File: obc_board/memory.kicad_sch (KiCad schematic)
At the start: 10 parts

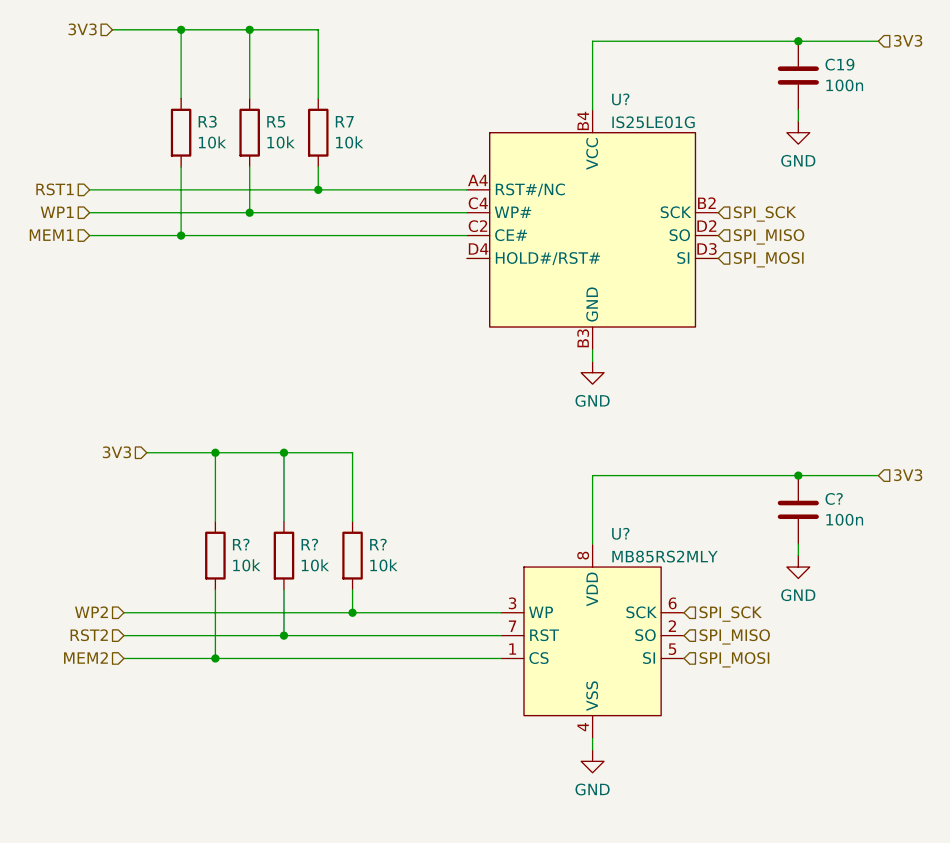
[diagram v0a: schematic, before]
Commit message: changed magnetorquer driver IC and changed power switch IC
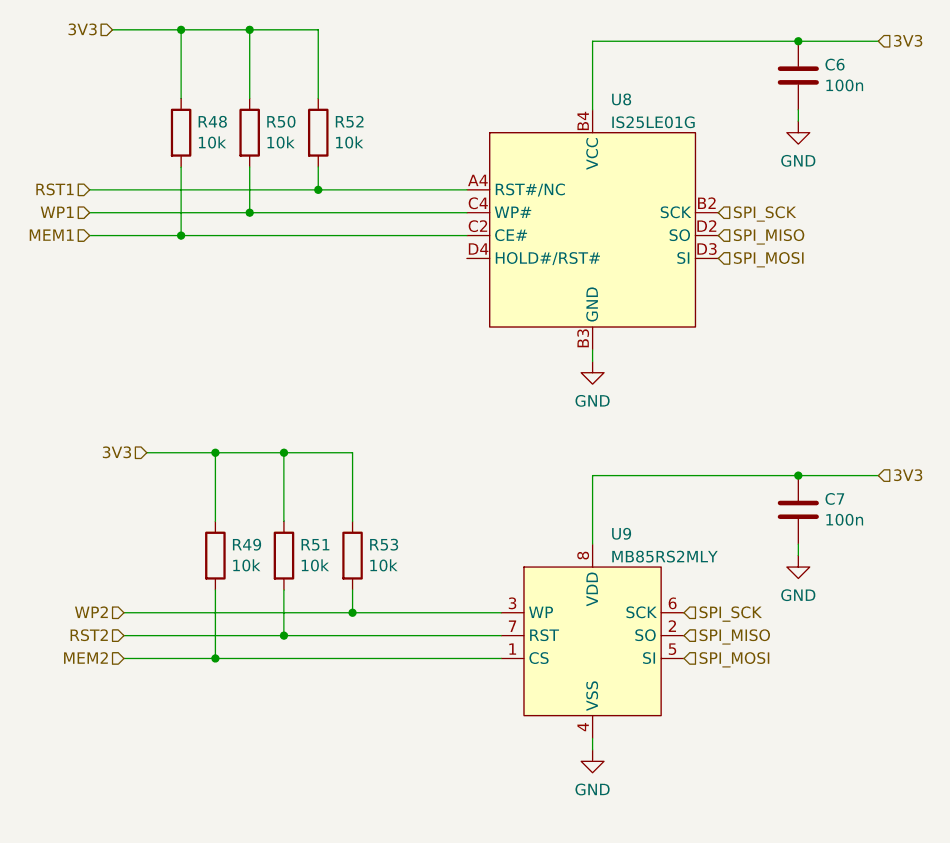
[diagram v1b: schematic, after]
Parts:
- gave numbers to parts that had none: 6
- renumbered C19 to C6, R3 to R48, R5 to R50, R7 to R52
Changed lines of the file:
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@@
   (symbol (lib_id "Device:C") (at 154.94 55.88 0) (unit 1)
     (in_bom yes) (on_board yes)
-    (property "Reference" "C19" (id 0) (at 157.861 54.7116 0)
+    (property "Reference" "C6" (id 0) (at 157.861 54.7116 0)
       (effects (font (size 1.27 1.27)) (justify left))
     )
@@
   (symbol (lib_id "Device:R") (at 101.6 62.23 0) (unit 1)
     (in_bom yes) (on_board yes)
-    (property "Reference" "R7" (id 0) (at 103.378 61.0616 0)
+    (property "Reference" "R52" (id 0) (at 103.378 61.0616 0)
       (effects (font (size 1.27 1.27)) (justify left))
     )
@@
   (symbol (lib_id "Device:R") (at 93.98 62.23 0) (unit 1)
     (in_bom yes) (on_board yes)
-    (property "Reference" "R5" (id 0) (at 95.758 61.0616 0)
+    (property "Reference" "R50" (id 0) (at 95.758 61.0616 0)
       (effects (font (size 1.27 1.27)) (justify left))
     )
@@
   (symbol (lib_id "Device:R") (at 86.36 62.23 0) (unit 1)
     (in_bom yes) (on_board yes)
-    (property "Reference" "R3" (id 0) (at 88.138 61.0616 0)
+    (property "Reference" "R48" (id 0) (at 88.138 61.0616 0)
       (effects (font (size 1.27 1.27)) (justify left))
     )
@@
   (symbol (lib_id "Device:C") (at 154.94 104.14 0) (unit 1)
     (in_bom yes) (on_board yes)
-    (property "Reference" "C?" (id 0) (at 157.861 102.9716 0)
+    (property "Reference" "C7" (id 0) (at 157.861 102.9716 0)
       (effects (font (size 1.27 1.27)) (justify left))
     )
@@
   (symbol (lib_id "power:GND") (at 154.94 109.22 0) (unit 1)
     (in_bom yes) (on_board yes) (fields_autoplaced)
-    (property "Reference" "#PWR?" (id 0) (at 154.94 115.57 0)
+    (property "Reference" "#PWR023" (id 0) (at 154.94 115.57 0)
       (effects (font (size 1.27 1.27)) hide)
     )
@@
   (symbol (lib_id "Device:R") (at 90.17 109.22 0) (unit 1)
     (in_bom yes) (on_board yes)
-    (property "Reference" "R?" (id 0) (at 91.948 108.0516 0)
+    (property "Reference" "R49" (id 0) (at 91.948 108.0516 0)
       (effects (font (size 1.27 1.27)) (justify left))
     )
@@
   (symbol (lib_name "MB85RS2MLY_1") (lib_id "cubesat_obc_lib:MB85RS2MLY") (at 132.08 119.38 0) (unit 1)
     (in_bom yes) (on_board yes) (fields_autoplaced)
-    (property "Reference" "U?" (id 0) (at 134.0994 106.841 0)
+    (property "Reference" "U9" (id 0) (at 134.0994 106.841 0)
       (effects (font (size 1.27 1.27)) (justify left))
     )
@@
   (symbol (lib_id "cubesat_obc_lib:IS25LE01G") (at 132.08 73.66 0) (unit 1)
     (in_bom yes) (on_board yes) (fields_autoplaced)
-    (property "Reference" "U?" (id 0) (at 134.0994 58.581 0)
+    (property "Reference" "U8" (id 0) (at 134.0994 58.581 0)
       (effects (font (size 1.27 1.27)) (justify left))
     )
@@
   (symbol (lib_id "power:GND") (at 132.08 130.81 0) (unit 1)
     (in_bom yes) (on_board yes) (fields_autoplaced)
-    (property "Reference" "#PWR?" (id 0) (at 132.08 137.16 0)
+    (property "Reference" "#PWR021" (id 0) (at 132.08 137.16 0)
       (effects (font (size 1.27 1.27)) hide)
     )
@@
   (symbol (lib_id "power:GND") (at 132.08 87.63 0) (unit 1)
     (in_bom yes) (on_board yes) (fields_autoplaced)
-    (property "Reference" "#PWR?" (id 0) (at 132.08 93.98 0)
+    (property "Reference" "#PWR020" (id 0) (at 132.08 93.98 0)
       (effects (font (size 1.27 1.27)) hide)
     )
@@
   (symbol (lib_id "Device:R") (at 105.41 109.22 0) (unit 1)
     (in_bom yes) (on_board yes)
-    (property "Reference" "R?" (id 0) (at 107.188 108.0516 0)
+    (property "Reference" "R53" (id 0) (at 107.188 108.0516 0)
       (effects (font (size 1.27 1.27)) (justify left))
     )
@@
   (symbol (lib_id "power:GND") (at 154.94 60.96 0) (unit 1)
     (in_bom yes) (on_board yes) (fields_autoplaced)
-    (property "Reference" "#PWR?" (id 0) (at 154.94 67.31 0)
+    (property "Reference" "#PWR022" (id 0) (at 154.94 67.31 0)
       (effects (font (size 1.27 1.27)) hide)
     )
@@
   (symbol (lib_id "Device:R") (at 97.79 109.22 0) (unit 1)
     (in_bom yes) (on_board yes)
-    (property "Reference" "R?" (id 0) (at 99.568 108.0516 0)
-      (effects (font (size 1.27 1.27)) (justify left))
-    )
+    (property "Reference" "R51" (id 0) (at 99.568 108.0516 0)
+      (effects (font (size 1.27 1.27)) (justify left))
+    )

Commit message: updated digikey part numbers and footprints
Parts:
- C6, C7: Digikey Part Number 490-16433-1-ND -> 399-6828-1-ND
- R48, R49, R50, R51, R52, R53: Digikey Part Number 311-10.0KLRCT-ND -> YAG3436CT-ND
- U8: footprint (none) -> cubesat_obc:TFBGA24_5X5_6X8; Digikey Part Number (none) -> 706-IS25LE01G-RILE-ND
- U9: footprint (none) -> Package_SO:SOIC-8_3.9x4.9mm_P1.27mm; Digikey Part Number (none) -> 865-MB85RS2MLYPNF-GS-AWE2-ND
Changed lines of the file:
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@@
       (effects (font (size 1.27 1.27)) hide)
     )
-    (property "Digikey Part Number" "490-16433-1-ND" (id 4) (at 154.94 55.88 0)
+    (property "Digikey Part Number" "399-6828-1-ND" (id 4) (at 154.94 55.88 0)
       (effects (font (size 1.27 1.27)) hide)
     )
@@
       (effects (font (size 1.27 1.27)) hide)
     )
-    (property "Digikey Part Number" "311-10.0KLRCT-ND" (id 4) (at 101.6 62.23 0)
+    (property "Digikey Part Number" "YAG3436CT-ND" (id 4) (at 101.6 62.23 0)
       (effects (font (size 1.27 1.27)) hide)
     )
@@
       (effects (font (size 1.27 1.27)) hide)
     )
-    (property "Digikey Part Number" "311-10.0KLRCT-ND" (id 4) (at 93.98 62.23 0)
+    (property "Digikey Part Number" "YAG3436CT-ND" (id 4) (at 93.98 62.23 0)
       (effects (font (size 1.27 1.27)) hide)
     )
@@
       (effects (font (size 1.27 1.27)) hide)
     )
-    (property "Digikey Part Number" "311-10.0KLRCT-ND" (id 4) (at 86.36 62.23 0)
+    (property "Digikey Part Number" "YAG3436CT-ND" (id 4) (at 86.36 62.23 0)
       (effects (font (size 1.27 1.27)) hide)
     )
@@
       (effects (font (size 1.27 1.27)) hide)
     )
-    (property "Digikey Part Number" "490-16433-1-ND" (id 4) (at 154.94 104.14 0)
+    (property "Digikey Part Number" "399-6828-1-ND" (id 4) (at 154.94 104.14 0)
       (effects (font (size 1.27 1.27)) hide)
     )
@@
       (effects (font (size 1.27 1.27)) hide)
     )
-    (property "Digikey Part Number" "311-10.0KLRCT-ND" (id 4) (at 90.17 109.22 0)
+    (property "Digikey Part Number" "YAG3436CT-ND" (id 4) (at 90.17 109.22 0)
       (effects (font (size 1.27 1.27)) hide)
     )
@@
       (effects (font (size 1.27 1.27)) (justify left))
     )
-    (property "Footprint" "" (id 2) (at 132.08 119.38 0)
-      (effects (font (size 1.27 1.27)) hide)
-    )
-    (property "Datasheet" "" (id 3) (at 132.08 119.38 0)
+    (property "Footprint" "Package_SO:SOIC-8_3.9x4.9mm_P1.27mm" (id 2) (at 132.08 119.38 0)
+      (effects (font (size 1.27 1.27)) hide)
+    )
+    (property "Datasheet" "https://www.fujitsu.com/uk/imagesgig5/MB85RS2MLY-DS501-00062-GS%20-0v1-E_13.pdf" (id 3) (at 132.08 119.38 0)
+      (effects (font (size 1.27 1.27)) hide)
+    )
+    (property "Digikey Part Number" "865-MB85RS2MLYPNF-GS-AWE2-ND" (id 4) (at 132.08 119.38 0)
       (effects (font (size 1.27 1.27)) hide)
     )
@@
       (effects (font (size 1.27 1.27)) (justify left))
     )
-    (property "Footprint" "" (id 2) (at 132.08 73.66 0)
-      (effects (font (size 1.27 1.27)) hide)
-    )
-    (property "Datasheet" "" (id 3) (at 132.08 73.66 0)
+    (property "Footprint" "cubesat_obc:TFBGA24_5X5_6X8" (id 2) (at 132.08 73.66 0)
+      (effects (font (size 1.27 1.27)) hide)
+    )
+    (property "Datasheet" "https://www.issi.com/WW/pdf/25LE-WE01G.pdf" (id 3) (at 132.08 73.66 0)
+      (effects (font (size 1.27 1.27)) hide)
+    )
+    (property "Digikey Part Number" "706-IS25LE01G-RILE-ND" (id 4) (at 132.08 73.66 0)
       (effects (font (size 1.27 1.27)) hide)
     )
@@
       (effects (font (size 1.27 1.27)) hide)
     )
-    (property "Digikey Part Number" "311-10.0KLRCT-ND" (id 4) (at 105.41 109.22 0)
+    (property "Digikey Part Number" "YAG3436CT-ND" (id 4) (at 105.41 109.22 0)
       (effects (font (size 1.27 1.27)) hide)
     )
@@
       (effects (font (size 1.27 1.27)) hide)
     )
-    (property "Digikey Part Number" "311-10.0KLRCT-ND" (id 4) (at 97.79 109.22 0)
-      (effects (font (size 1.27 1.27)) hide)
-    )
+    (property "Digikey Part Number" "YAG3436CT-ND" (id 4) (at 97.79 109.22 0)
+      (effects (font (size 1.27 1.27)) hide)
+    )

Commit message: routed most of board
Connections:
- net at U8.A2 (NC), U8.A3 (NC), U8.A5 (NC)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: no longer U8.E6 (NC)
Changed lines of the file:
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@@
     (pin "2")
   )
-  (symbol (lib_name "MB85RS2MLY_1") (lib_id "cubesat_obc_lib:MB85RS2MLY") (at 132.08 119.38 0) (unit 1)
+  (symbol (lib_id "cubesat_obc_lib:MB85RS2MLY") (at 132.08 119.38 0) (unit 1)
     (in_bom yes) (on_board yes) (fields_autoplaced)
     (property "Reference" "U9" (id 0) (at 134.0994 106.841 0)
@@
     (pin "E4")
     (pin "E5")
-    (pin "E6")
   )
   (symbol (lib_id "power:GND") (at 132.08 130.81 0) (unit 1)

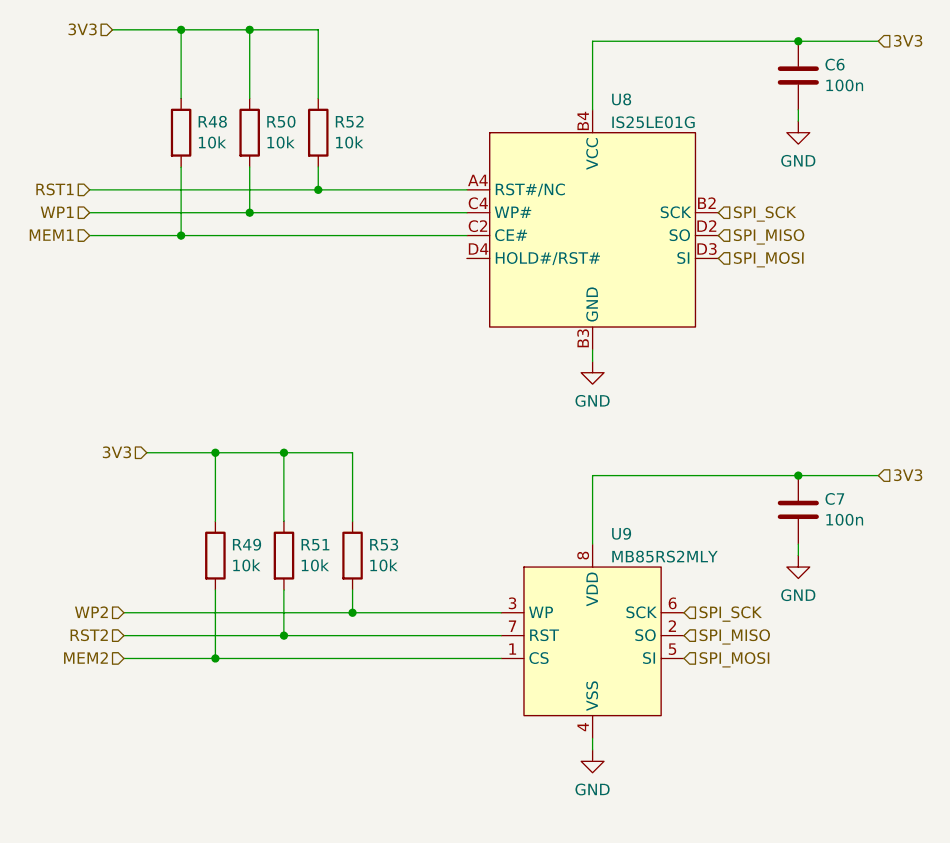
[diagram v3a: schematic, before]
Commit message: fixed SPI pins mixup for memory, switched to MRAM instead of FRAM
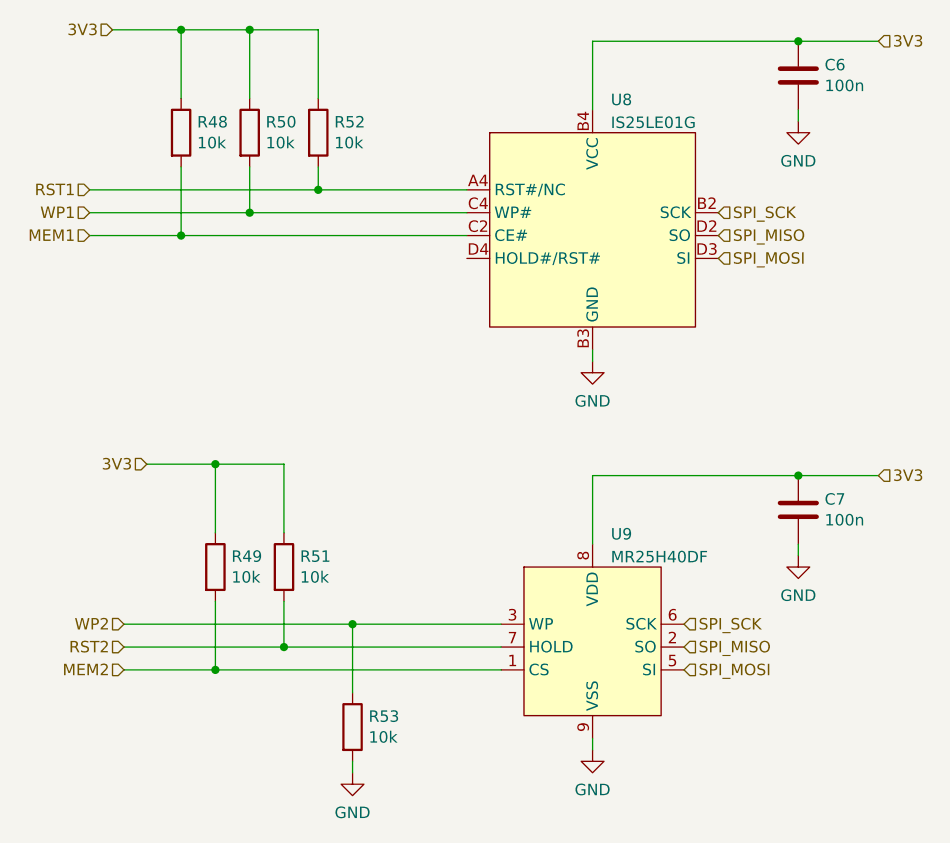
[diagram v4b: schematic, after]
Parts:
- removed U9: MB85RS2MLY, Package_SO:SOIC-8_3.9x4.9mm_P1.27mm, symbol cubesat_obc_lib:MB85RS2MLY
- added U9: MR25H40DF, Package_DFN_QFN:DFN-8-1EP_6x5mm_P1.27mm_EP2x2mm, symbol cubesat_obc_lib:MR25H40DF
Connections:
- net 3V3: now also U9.8 (VDD); no longer R53.1
- net GND: now also R53.2, U9.4 (VSS), U9.9 (VSS)
- net MEM2: now also U9.1 (CS)
- net RST2: now also U9.7 (HOLD)
- net SPI_MISO: now also U9.2 (SO)
- net SPI_MOSI: now also U9.5 (SI)
- net SPI_SCK: now also U9.6 (SCK)
- net WP2: now also R53.1, U9.3 (WP); no longer R53.2
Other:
- moved on the sheet: R49, R51, R53
